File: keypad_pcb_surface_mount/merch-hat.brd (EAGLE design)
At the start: 65 x 56 mm, 26 parts, among them U2 ATMEGA328P_TQFP, Y2 16MHZ

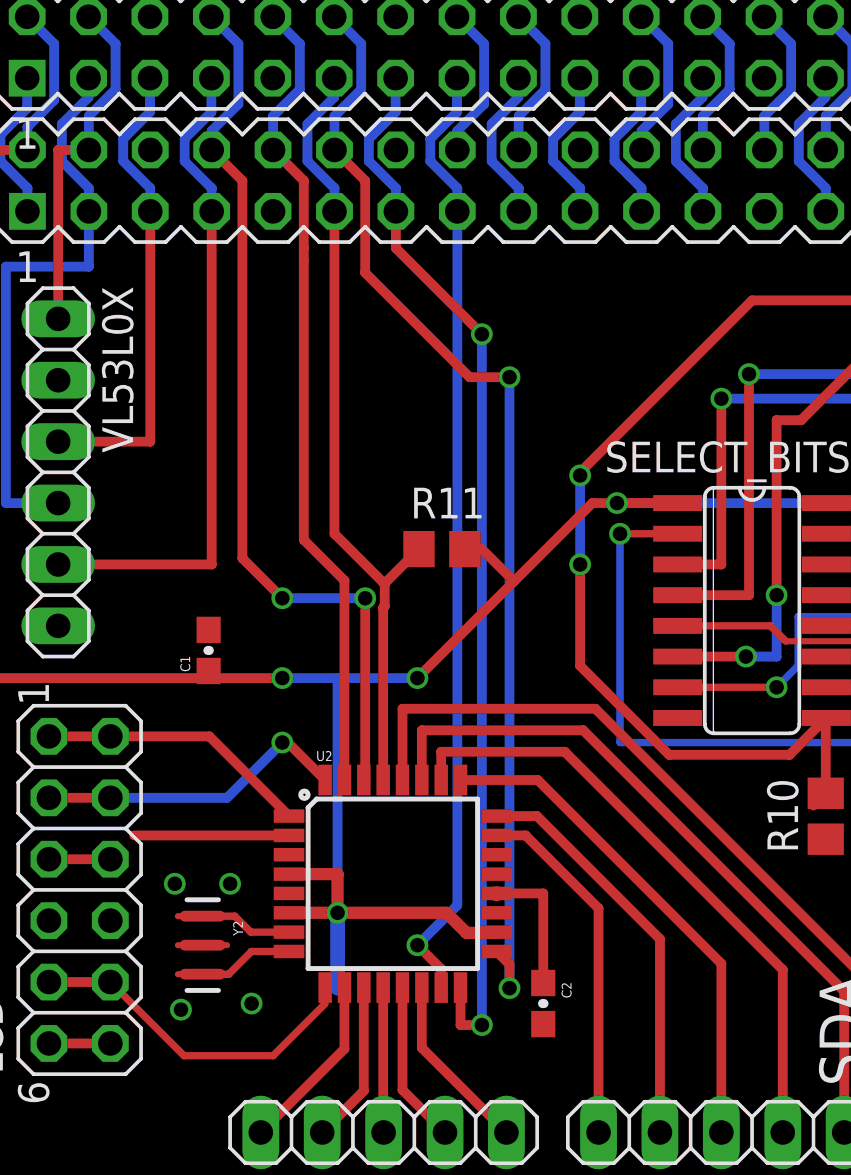
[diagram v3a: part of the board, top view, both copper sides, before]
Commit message: Add Limit Switch Interface
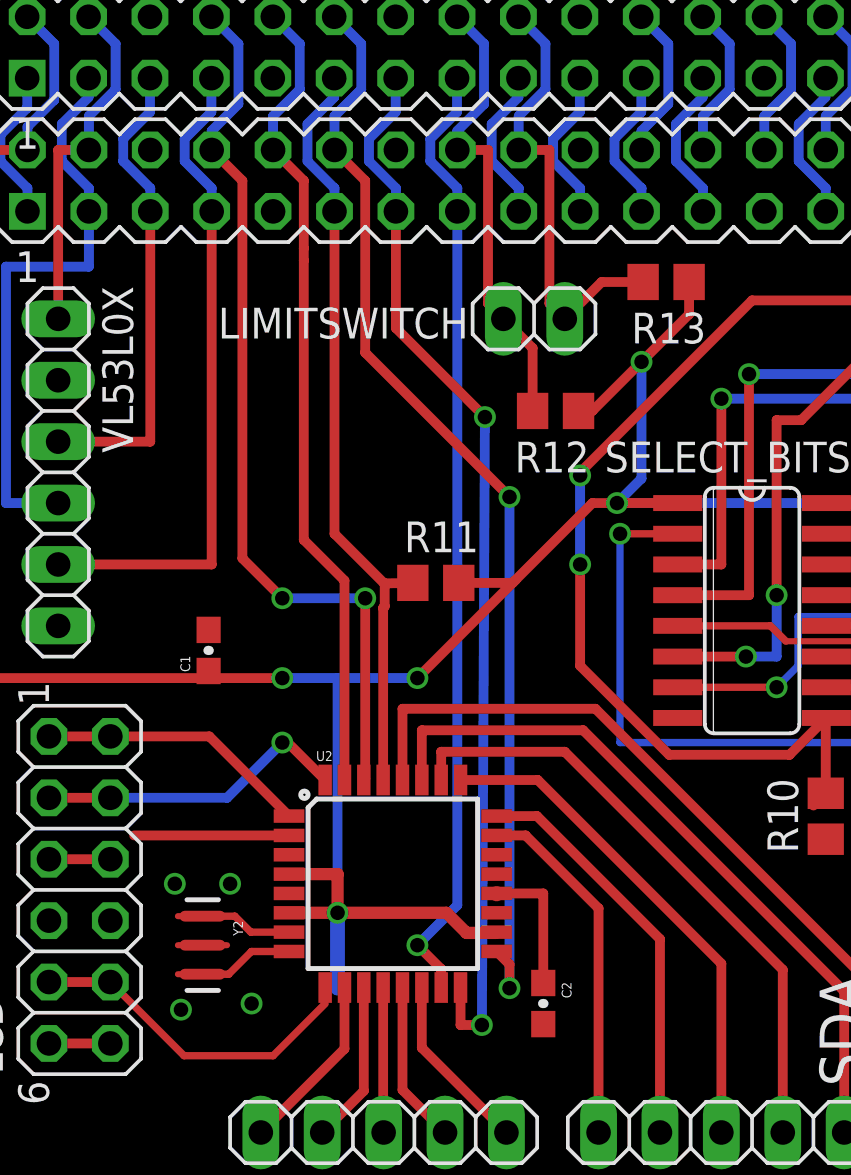
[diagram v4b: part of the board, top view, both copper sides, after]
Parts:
- added LIMITSWITCH: (no value), pinhead:1X02
- added R12, R13: 3.3k, resistor:R0805
- moved R11 1.42 mm to (25.3, 30.4)
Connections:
- net +5V: now also R12.1, R13.1
- net GPIO23: now also LIMITSWITCH.2, R12.2
- net GPIO24: now also LIMITSWITCH.1, R13.2
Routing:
- net +5V: track 188.5 -> 202.2 mm, vias 7 -> 8
- net GPIO23: track 6.43 -> 19.3 mm
- net GPIO24: track 6.43 -> 18.8 mm
- net ICSP_SCK: track 46.8 -> 45.8 mm
- net ICSP_RESET: track 32.9 -> 32.1 mm
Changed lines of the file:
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@@
 <?xml version="1.0" encoding="utf-8"?>
 <!DOCTYPE eagle SYSTEM "eagle.dtd">
-<eagle version="8.0.1">
+<eagle version="8.1.0">
 <drawing>
 <settings>
@@
 <attribute name="VALUE" x="16.764" y="4.445" size="1.27" layer="27"/>
 </element>
-<element name="R11" library="resistor" package="R0805" value="3.3k" x="25.527" y="31.75" smashed="yes" rot="R180">
-<attribute name="NAME" x="27.305" y="34.29" size="1.27" layer="25" rot="R180"/>
-<attribute name="VALUE" x="26.162" y="34.29" size="1.27" layer="27" rot="R180"/>
+<element name="R11" library="resistor" package="R0805" value="3.3k" x="25.273" y="30.353" smashed="yes" rot="R180">
+<attribute name="NAME" x="27.051" y="32.893" size="1.27" layer="25" rot="R180"/>
+<attribute name="VALUE" x="25.908" y="32.893" size="1.27" layer="27" rot="R180"/>
 </element>
 <element name="C1" library="SparkFun-Capacitors" package="0603-CAP" value="0.1uF" x="15.875" y="27.559" rot="R90"/>
+<element name="R12" library="resistor" package="R0805" value="3.3k" x="30.226" y="37.465" smashed="yes" rot="R180">
+<attribute name="NAME" x="31.623" y="36.195" size="1.27" layer="25" rot="R180"/>
+<attribute name="VALUE" x="30.861" y="40.005" size="1.27" layer="27" rot="R180"/>
+</element>
+<element name="R13" library="resistor" package="R0805" value="3.3k" x="34.798" y="42.799" smashed="yes" rot="R180">
+<attribute name="NAME" x="36.449" y="41.529" size="1.27" layer="25" rot="R180"/>
+<attribute name="VALUE" x="35.433" y="45.339" size="1.27" layer="27" rot="R180"/>
+</element>
+<element name="LIMITSWITCH" library="pinhead" package="1X02" value="" x="29.337" y="41.275" smashed="yes" rot="R180">
+<attribute name="NAME" x="26.6192" y="41.7322" size="1.27" layer="25" ratio="10" rot="R180"/>
+<attribute name="VALUE" x="31.877" y="44.45" size="1.27" layer="27" rot="R180"/>
+</element>
 </elements>
 <signals>
@@
 <wire x1="21.209" y1="26.416" x2="24.511" y2="26.416" width="0.4064" layer="16"/>
 <via x="24.511" y="26.416" extent="1-16" drill="0.6"/>
-<wire x1="28.5115" y1="30.4165" x2="24.511" y2="26.416" width="0.4064" layer="1"/>
-<wire x1="28.5115" y1="30.4165" x2="31.75" y2="33.655" width="0.4064" layer="1"/>
+<wire x1="28.575" y1="30.48" x2="31.75" y2="33.655" width="0.4064" layer="1"/>
+<wire x1="28.575" y1="30.48" x2="24.511" y2="26.416" width="0.4064" layer="1"/>
 <wire x1="31.75" y1="33.655" x2="32.766" y2="33.655" width="0.4064" layer="1"/>
 <via x="32.766" y="33.655" extent="1-16" drill="0.6"/>
@@
 <wire x1="32.766" y1="33.655" x2="43.307" y2="33.655" width="0.4064" layer="16"/>
 <contactref element="R11" pad="1"/>
-<wire x1="26.477" y1="31.75" x2="27.178" y2="31.75" width="0.4064" layer="1"/>
-<wire x1="27.178" y1="31.75" x2="28.5115" y2="30.4165" width="0.4064" layer="1"/>
 <contactref element="C1" pad="1"/>
 <wire x1="15.875" y1="26.709" x2="15.875" y2="26.416" width="0.4064" layer="1"/>
+<contactref element="R12" pad="1"/>
+<contactref element="R13" pad="1"/>
+<wire x1="35.748" y1="42.799" x2="35.748" y2="41.463" width="0.4064" layer="1"/>
+<wire x1="33.782" y1="39.497" x2="35.748" y2="41.463" width="0.4064" layer="1"/>
+<via x="33.782" y="39.497" extent="1-16" drill="0.6" shape="square"/>
+<wire x1="33.782" y1="39.497" x2="33.782" y2="34.671" width="0.4064" layer="16"/>
+<wire x1="33.782" y1="34.671" x2="32.766" y2="33.655" width="0.4064" layer="16"/>
+<wire x1="31.176" y1="37.465" x2="31.75" y2="37.465" width="0.4064" layer="1"/>
+<wire x1="31.75" y1="37.465" x2="33.782" y2="39.497" width="0.4064" layer="1"/>
+<wire x1="26.223" y1="30.353" x2="28.448" y2="30.353" width="0.4064" layer="1"/>
+<wire x1="28.448" y1="30.353" x2="28.575" y2="30.48" width="0.4064" layer="1"/>
 <wire x1="8.382" y1="48.26" x2="9.652" y2="48.26" width="0" layer="19" extent="1-16"/>
 </signal>
@@
 <wire x1="22.1876" y1="52.6524" x2="22.1876" y2="50.76706875" width="0.4064" layer="16"/>
 <wire x1="21.082" y1="48.26" x2="22.352" y2="46.99" width="0.4064" layer="1"/>
-<wire x1="22.352" y1="43.18" x2="22.352" y2="46.99" width="0.4064" layer="1"/>
 <wire x1="27.7876" y1="15.107" x2="28.321" y2="14.5736" width="0.4064" layer="1"/>
 <wire x1="28.321" y1="14.5736" x2="28.321" y2="13.589" width="0.4064" layer="1"/>
 <via x="28.321" y="13.589" extent="1-16" drill="0.6"/>
-<wire x1="28.321" y1="13.589" x2="28.321" y2="38.862" width="0.4064" layer="16"/>
-<via x="28.321" y="38.862" extent="1-16" drill="0.6"/>
-<wire x1="28.321" y1="38.862" x2="26.67" y2="38.862" width="0.4064" layer="1"/>
-<wire x1="26.67" y1="38.862" x2="22.352" y2="43.18" width="0.4064" layer="1"/>
+<wire x1="28.321" y1="13.589" x2="28.321" y2="33.909" width="0.4064" layer="16"/>
+<via x="28.321" y="33.909" extent="1-16" drill="0.6"/>
+<wire x1="22.352" y1="39.878" x2="28.321" y2="33.909" width="0.4064" layer="1"/>
+<wire x1="22.352" y1="46.99" x2="22.352" y2="39.878" width="0.4064" layer="1"/>
 </signal>
 <signal name="N$29">
@@
 <wire x1="26.295" y1="12.065" x2="27.178" y2="12.065" width="0.4064" layer="1"/>
 <via x="27.178" y="12.065" extent="1-16" drill="0.6"/>
-<wire x1="27.178" y1="12.065" x2="27.178" y2="40.64" width="0.4064" layer="16"/>
-<via x="27.178" y="40.64" extent="1-16" drill="0.6"/>
-<wire x1="27.178" y1="40.64" x2="23.622" y2="44.196" width="0.4064" layer="1"/>
-<wire x1="23.622" y1="44.196" x2="23.622" y2="45.72" width="0.4064" layer="1"/>
+<wire x1="27.178" y1="12.065" x2="27.305" y2="37.211" width="0.4064" layer="16"/>
+<via x="27.305" y="37.211" extent="1-16" drill="0.6"/>
+<wire x1="27.305" y1="37.211" x2="23.622" y2="40.894" width="0.4064" layer="1"/>
+<wire x1="23.622" y1="40.894" x2="23.622" y2="45.72" width="0.4064" layer="1"/>
 </signal>
 <signal name="ICSP_MOSI">
@@
 <contactref element="R11" pad="2"/>
 <wire x1="23.16" y1="30.307" x2="23.16" y2="30.333" width="0.4064" layer="1"/>
-<wire x1="23.16" y1="30.333" x2="24.577" y2="31.75" width="0.4064" layer="1"/>
+<wire x1="23.16" y1="30.333" x2="24.323" y2="30.353" width="0.4064" layer="1"/>
 </signal>
 <signal name="VCC">
@@
 <wire x1="28.69" y1="53.77" x2="29.8076" y2="52.6524" width="0.4064" layer="16"/>
 <wire x1="29.8076" y1="52.6524" x2="29.8076" y2="50.76706875" width="0.4064" layer="16"/>
+<contactref element="R13" pad="2"/>
+<contactref element="LIMITSWITCH" pad="1"/>
+<wire x1="29.972" y1="48.26" x2="28.702" y2="48.26" width="0.4064" layer="1"/>
+<wire x1="29.972" y1="41.91" x2="30.607" y2="41.275" width="0.4064" layer="1"/>
+<wire x1="29.972" y1="41.91" x2="29.972" y2="48.26" width="0.4064" layer="1"/>
+<wire x1="30.607" y1="41.275" x2="32.131" y2="42.799" width="0.4064" layer="1"/>
+<wire x1="32.131" y1="42.799" x2="33.848" y2="42.799" width="0.4064" layer="1"/>
 </signal>
 <signal name="GPIO23">
@@
 <wire x1="27.2676" y1="52.6524" x2="27.2676" y2="50.1558625" width="0.4064" layer="16"/>
 <wire x1="27.2676" y1="50.1558625" x2="26.162" y2="49.0502625" width="0.4064" layer="16"/>
+<contactref element="R12" pad="2"/>
+<contactref element="LIMITSWITCH" pad="2"/>
+<wire x1="27.432" y1="48.26" x2="26.162" y2="48.26" width="0.4064" layer="1"/>
+<wire x1="27.432" y1="41.91" x2="28.067" y2="41.275" width="0.4064" layer="1"/>
+<wire x1="27.432" y1="41.91" x2="27.432" y2="48.26" width="0.4064" layer="1"/>
+<wire x1="28.067" y1="41.275" x2="29.276" y2="40.066" width="0.4064" layer="1"/>
+<wire x1="29.276" y1="40.066" x2="29.276" y2="37.465" width="0.4064" layer="1"/>
 </signal>
 <signal name="GPIO11">

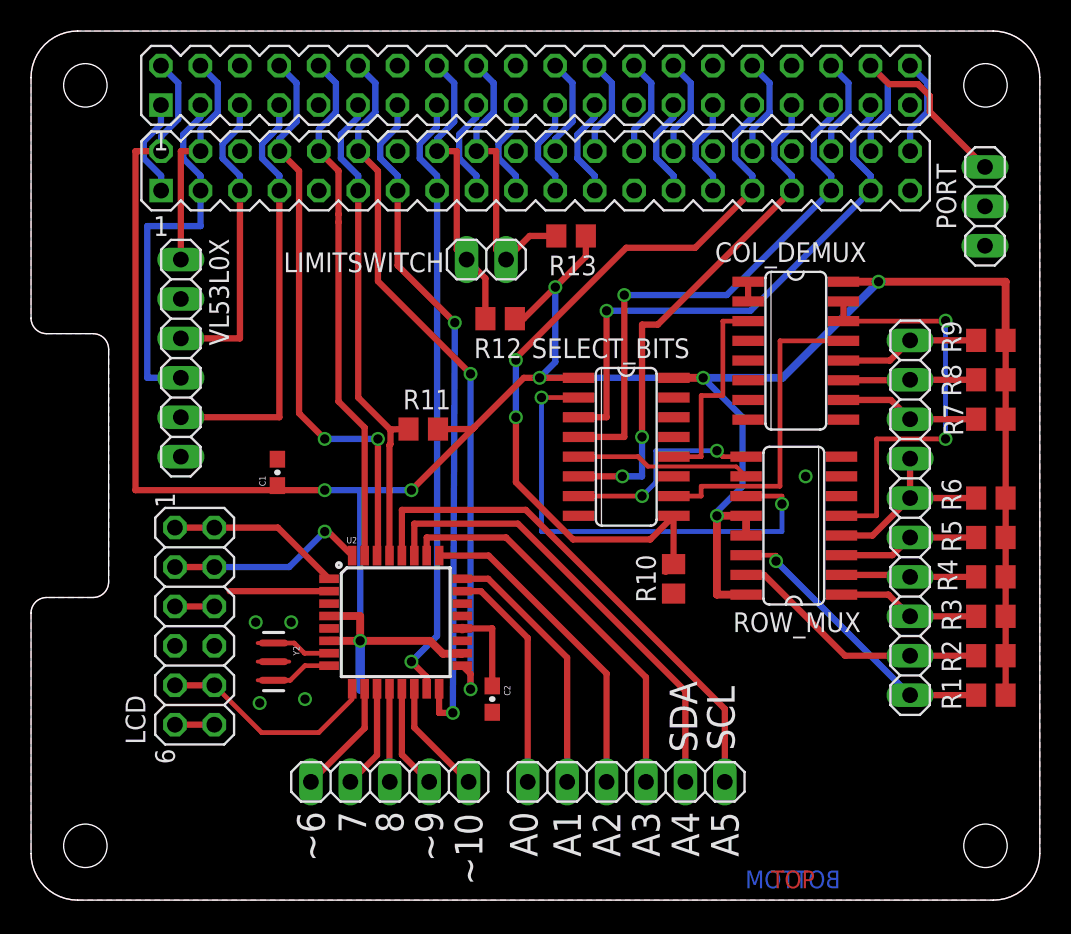
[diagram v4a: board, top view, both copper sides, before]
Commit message: Add Port Sensor Labels
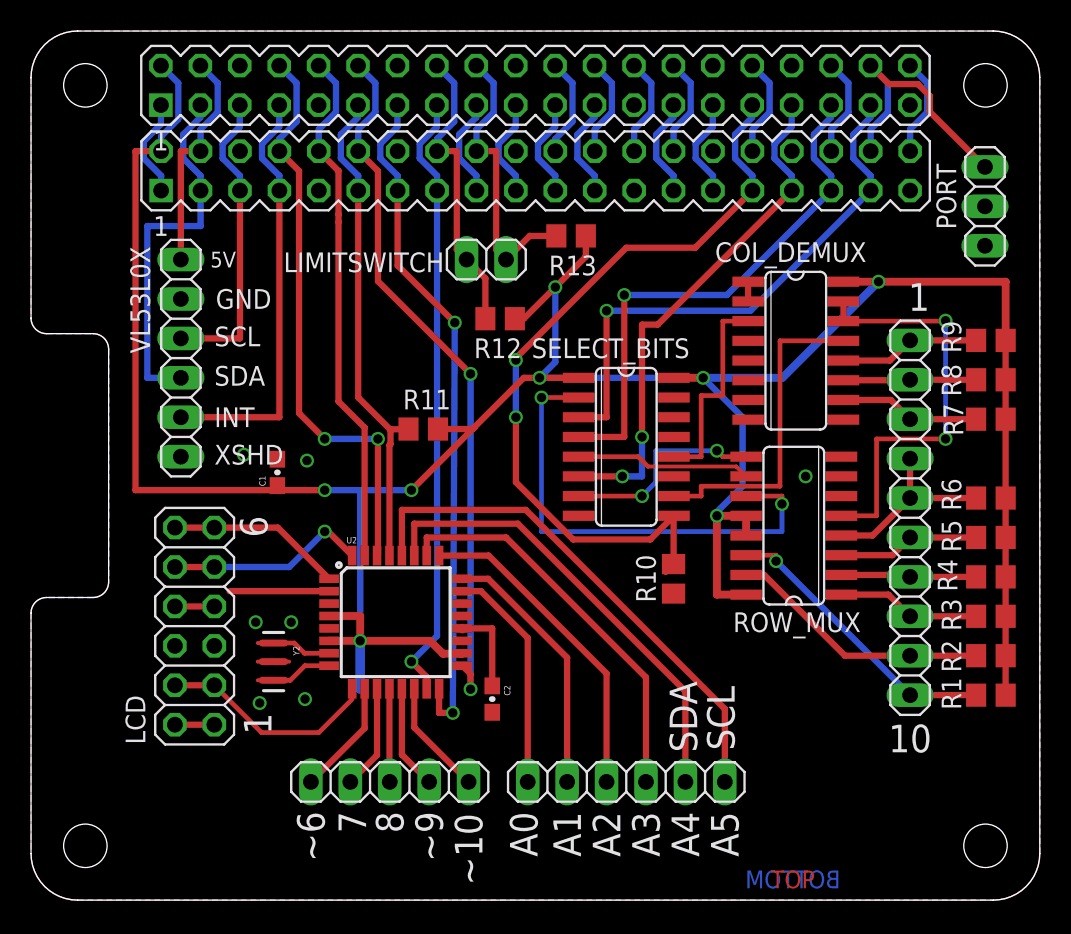
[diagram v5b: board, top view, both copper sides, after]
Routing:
- net GND: vias 5 -> 7
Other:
- board text added: "1"
- board text added: "10"
- board text added: "5V"
- board text added: "6"
- board text added: "GND"
- board text added: "INT"
- board text added: "XSHD"
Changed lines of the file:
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@@
 <text x="42.926" y="9.525" size="1.778" layer="21" rot="R90">SDA</text>
 <text x="45.339" y="9.652" size="1.778" layer="21" rot="R90">SCL</text>
+<text x="13.716" y="12.065" size="1.778" layer="21" rot="R270">1</text>
+<text x="13.462" y="24.765" size="1.778" layer="21" rot="R270">6</text>
+<text x="56.515" y="37.973" size="1.778" layer="21">1</text>
+<text x="55.245" y="9.525" size="1.778" layer="21">10</text>
+<text x="13.208" y="41.783" size="1.016" layer="21" rot="R180">5V</text>
+<text x="15.494" y="39.37" size="1.27" layer="21" rot="R180">GND
+</text>
+<text x="11.811" y="35.687" size="1.27" layer="21">SCL</text>
+<text x="11.811" y="33.147" size="1.27" layer="21">SDA</text>
+<text x="11.811" y="30.48" size="1.27" layer="21">INT</text>
+<text x="11.811" y="28.067" size="1.27" layer="21">XSHD</text>
 </plain>
 <attributes>
@@
 <attribute name="VALUE" x="64.1096" y="36.703" size="1.27" layer="27" ratio="10" rot="R180"/>
 </element>
-<element name="VL53L0X" library="pinhead" package="1X06" value="VL53L0X" x="9.652" y="34.925" rot="R270"/>
+<element name="VL53L0X" library="pinhead" package="1X06" value="VL53L0X" x="9.652" y="34.925" smashed="yes" rot="R270">
+<attribute name="NAME" x="6.4008" y="42.1132" size="1.27" layer="25" ratio="10" rot="R270"/>
+<attribute name="VALUE" x="6.477" y="42.545" size="1.27" layer="27" rot="R270"/>
+</element>
 <element name="PORT" library="pinhead" package="1X03" value="Sensor Port" x="61.468" y="44.704" smashed="yes" rot="R270">
 <attribute name="NAME" x="58.3438" y="47.4472" size="1.27" layer="25" ratio="10" rot="R270"/>
@@
 <contactref element="GPIO1" pad="34"/>
 <contactref element="C1" pad="2"/>
+<via x="13.716" y="28.702" extent="1-16" drill="0.6" shape="square"/>
+<via x="17.78" y="28.321" extent="1-16" drill="0.6" shape="square"/>
 </signal>
 <signal name="GPIO20">
@@
 </board>
 </drawing>
+<compatibility>
+<note version="6.3" minversion="6.2.2" severity="warning">
+Since Version 6.2.2 text objects can contain more than one line,
+which will not be processed correctly with this version.
+</note>
+</compatibility>
 </eagle>
